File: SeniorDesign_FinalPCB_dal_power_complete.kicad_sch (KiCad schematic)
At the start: 75 parts, among them J1 5000, J10 5000, J2 5000, J3 5000, J4 5000, J5 5000, J6 5000, J7 5000, J8 5000, J9 5000, U1 Transducer, U10 Transducer, U11 Transducer, U12 Transducer, U13 Transducer, U14 Transducer, U15 Transducer, U16 Transducer, U17 Transducer, U18 Transducer, U19 Transducer, U2 Transducer, U20 Transducer, U21 Transducer, U22 Transducer, U23 Transducer, U24 Transducer, U25 Transducer, U26 Transducer, U27 Transducer, U28 Transducer, U29 Transducer, U3 Transducer, U30 Transducer, U31 Transducer, U32 Transducer, U33 Transducer, U34 Transducer, U35 Transducer, U36 Transducer, U37 Transducer, U38 Transducer, U39 Transducer, U4 Transducer, U40 Transducer, U41 Transducer, U42 Transducer, U43 Transducer, U44 Transducer, U45 Transducer, U46 Transducer, U47 Transducer, U48 Transducer, U49 Transducer, U5 Transducer, U50 Transducer, U51 Transducer, U52 Transducer, U53 Transducer, U54 Transducer, U55 Transducer, U56 Transducer, U57 Transducer, U58 Transducer, U59 Transducer, U6 Transducer, U60 Transducer, U61 Transducer, U62 Transducer, U63 Transducer, U64 Transducer, U65 CMOD_A7, U7 Transducer, U8 Transducer, U9 Transducer

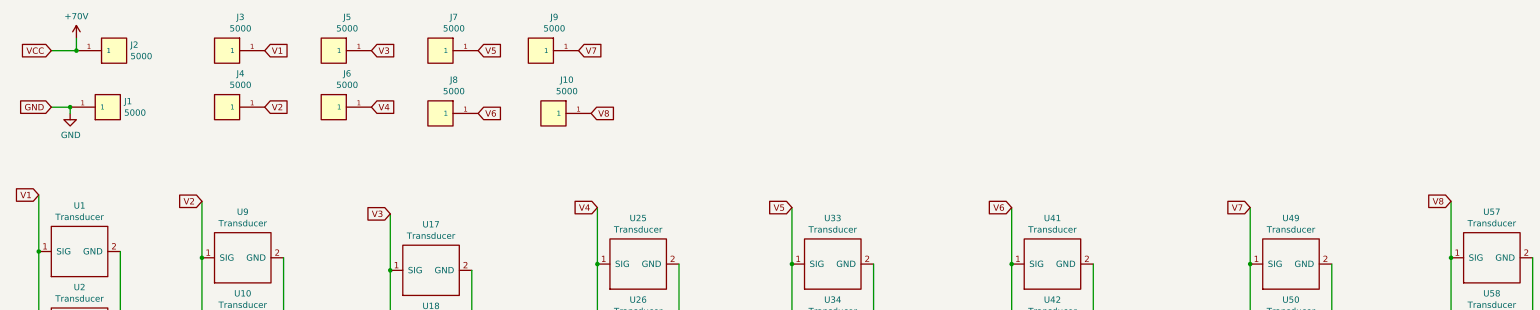
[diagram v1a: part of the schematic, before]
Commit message: Fixed transducer trace widths and via net names.
Also adds WELAC logo and silkscreen board name + contributors
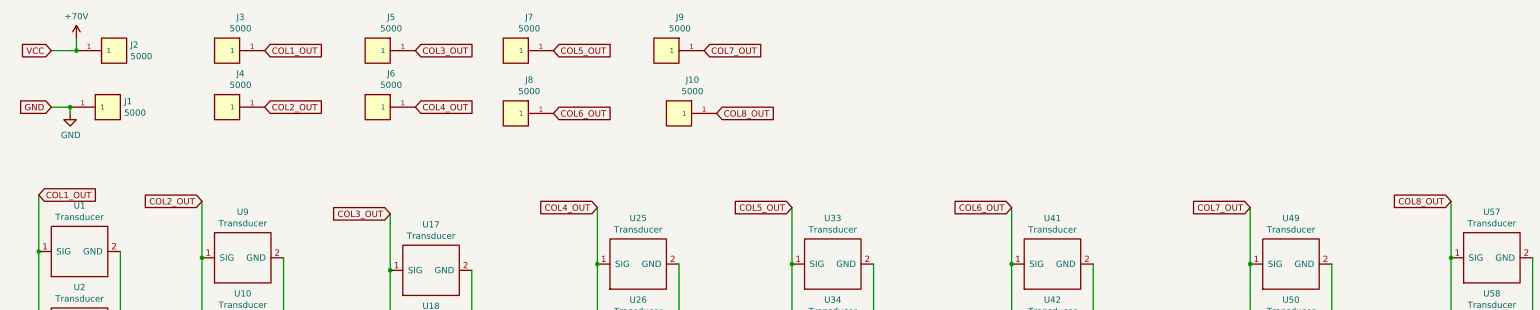
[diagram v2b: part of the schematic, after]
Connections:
- net V1 renamed COL1_OUT
- net V2 renamed COL2_OUT
- net V3 renamed COL3_OUT
- net V4 renamed COL4_OUT
- net V5 renamed COL5_OUT
- net V6 renamed COL6_OUT
- net V7 renamed COL7_OUT
- net V8 renamed COL8_OUT
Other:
- moved on the sheet: J10, J5, J6, J7, J8, J9

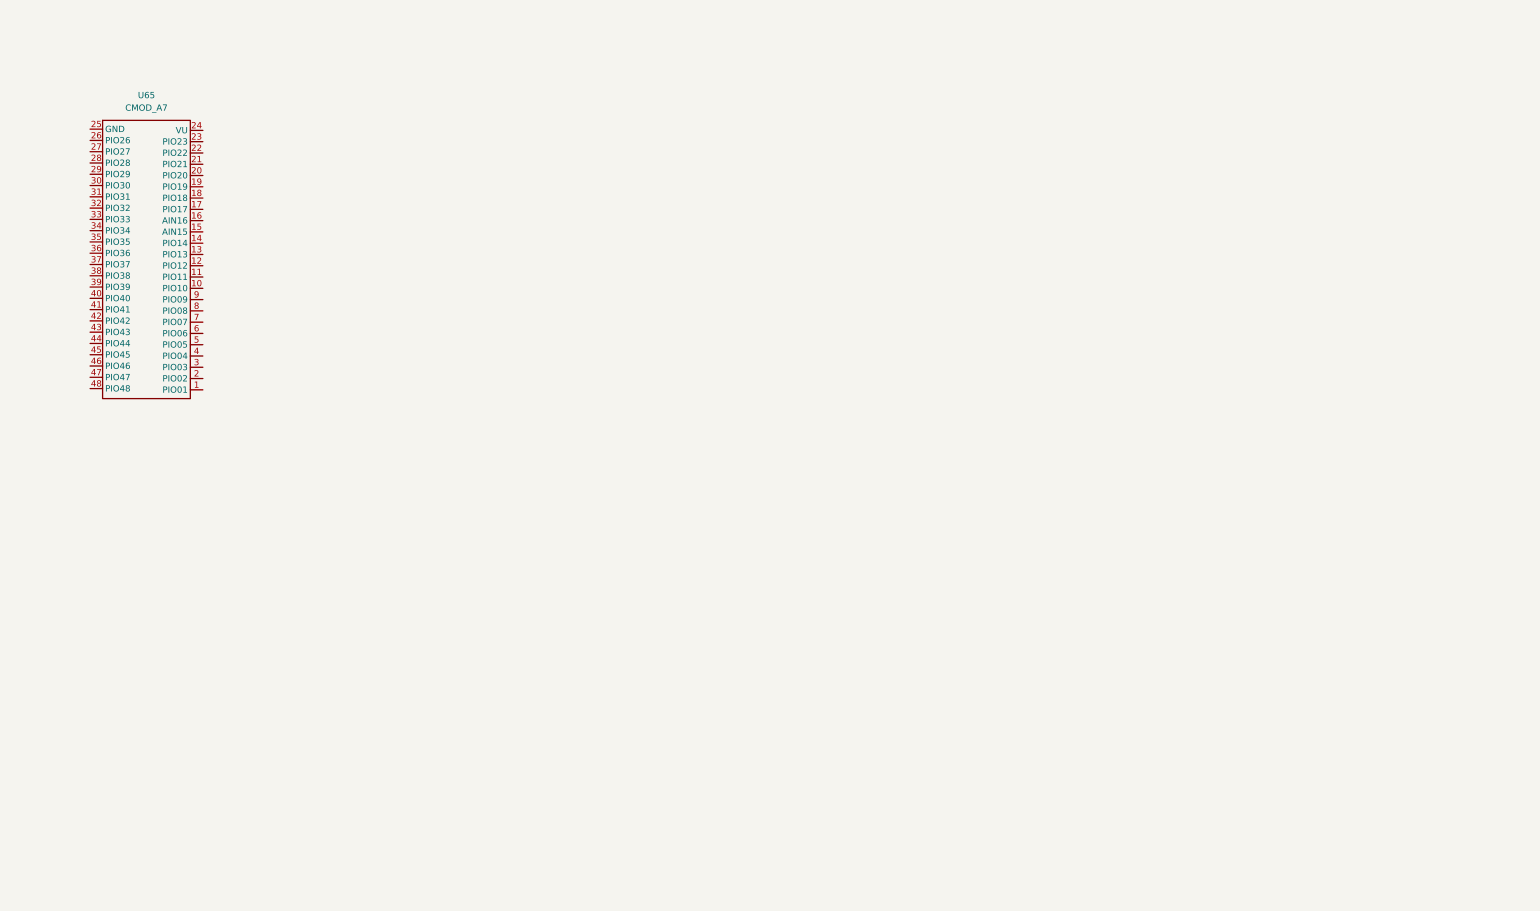
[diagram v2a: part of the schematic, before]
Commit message: all major components added, routing underway
added and fixed some component footprints. routed column signals and designed/layout of audio amplifier and power supply. NEED TO CHECK CAP VOLTAGES
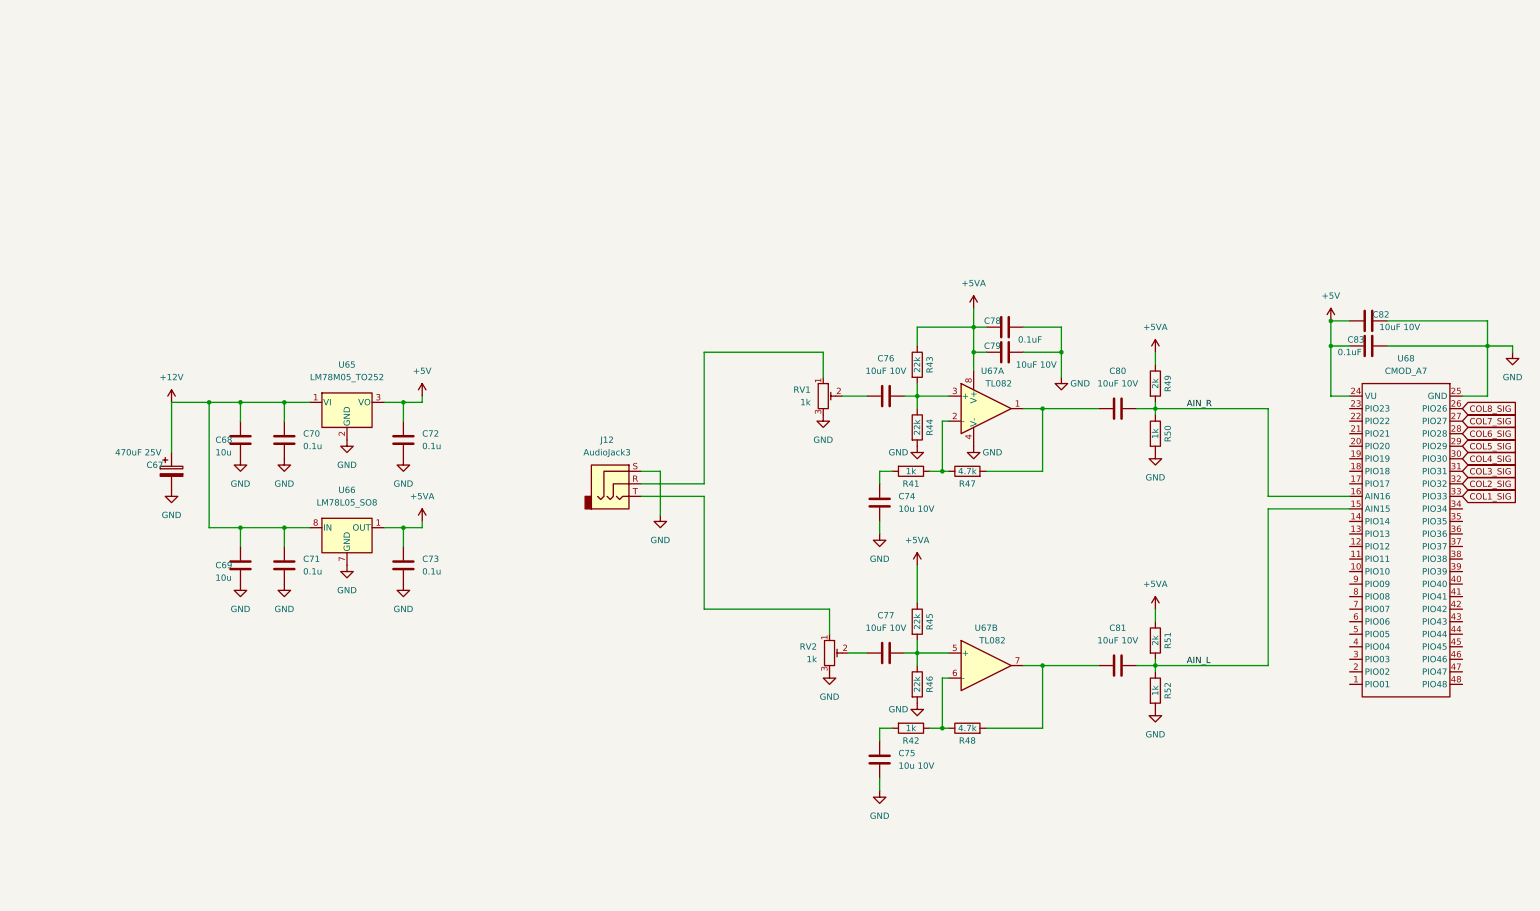
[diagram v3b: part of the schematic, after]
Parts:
- removed U65: CMOD_A7, SeniorDesign:CMOD A7, symbol SeniorDesign:CMOD_A7
- added C67: 470uF 25V, Capacitor_SMD:CP_Elec_10x10, symbol Device:C_Polarized
- added C68, C69: 10u, Capacitor_SMD:C_0603_1608Metric, symbol Device:C
- added C70, C71, C72, C73: 0.1u, Capacitor_SMD:C_0603_1608Metric, symbol Device:C
- added C74, C75: 10u 10V, Capacitor_SMD:C_0603_1608Metric, symbol Device:C
- added C76, C77, C79, C80, C81, C82: 10uF 10V, Capacitor_SMD:C_0603_1608Metric, symbol Device:C
- added C78, C83: 0.1uF, Capacitor_SMD:C_0603_1608Metric, symbol Device:C
- added J12: AudioJack3, Connector_Audio:Jack_3.5mm_CUI_SJ-3523-SMT_Horizontal, symbol Connector:AudioJack3
- added R41, R42, R50, R52: 1k, Resistor_SMD:R_0603_1608Metric, symbol Device:R
- added R43, R44, R45, R46: 22k, Resistor_SMD:R_0603_1608Metric, symbol Device:R
- added R47, R48: 4.7k, Resistor_SMD:R_0603_1608Metric, symbol Device:R
- added R49, R51: 2k, Resistor_SMD:R_0603_1608Metric, symbol Device:R
- added RV1, RV2: 1k, Potentiometer_SMD:Potentiometer_Bourns_3314J_Vertical, symbol Device:R_Potentiometer_Trim
- added U65: LM78M05_TO252, Package_TO_SOT_SMD:TO-252-2, symbol Regulator_Linear:LM78M05_TO252
- added U66: LM78L05_SO8, Package_SO:SOIC-8_3.9x4.9mm_P1.27mm, symbol Regulator_Linear:LM78L05_SO8
- added U67: TL082, Package_DIP:DIP-8_W7.62mm_LongPads, symbol Amplifier_Operational:TL082
- added U68: CMOD_A7, Senior:CMOD A7, symbol SeniorDesign:CMOD_A7
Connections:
- net GND: now also C67.2, C68.2, C69.2, C70.2, C71.2, C72.2, C73.2, C74.1, C75.1, C78.2, C79.2, C82.2, C83.2, J12.S, R44.2, R46.2, R50.2, R52.2, RV1.3, RV2.3, U65.2 (GND), U66.2 (GND), U66.3 (GND), U66.6 (GND), U66.7 (GND), U67.4 (V-), U68.25 (GND)
- new net: C81.1, R48.2, U67.7
- new net: R42.1, R48.1, U67.6 (-)
- new net: C77.2, R45.2, R46.1, U67.5 (+)
- new net: C76.2, R43.2, R44.1, U67.3 (+)
- new net: C80.1, R47.2, U67.1
- new net: R41.1, R47.1, U67.2 (-)
- new net: C77.1, RV2.2
- new net: J12.R, RV1.1
- new net: C76.1, RV1.2
- new net: C74.2, R41.2
- new net: C75.2, R42.2
- new net: J12.T, RV2.1
- new net +12V: C67.1, C68.1, C69.1, C70.1, C71.1, U65.1 (VI), U66.8 (IN)
- new net +5V: C72.1, C82.1, C83.1, U65.3 (VO), U68.24 (VU)
- new net +5VA: C73.1, C78.1, C79.1, R43.1, R45.1, R49.1, R51.1, U66.1 (OUT), U67.8 (V+)
- new net AIN_L: C81.2, R51.2, R52.1, U68.15 (AIN15)
- new net AIN_R: C80.2, R49.2, R50.1, U68.16 (AIN16)
- new net COL1_SIG: U68.33 (PIO33)
- new net COL2_SIG: U68.32 (PIO32)
- new net COL3_SIG: U68.31 (PIO31)
- new net COL4_SIG: U68.30 (PIO30)
- new net COL5_SIG: U68.29 (PIO29)
- new net COL6_SIG: U68.28 (PIO28)
- new net COL7_SIG: U68.27 (PIO27)
- new net COL8_SIG: U68.26 (PIO26)

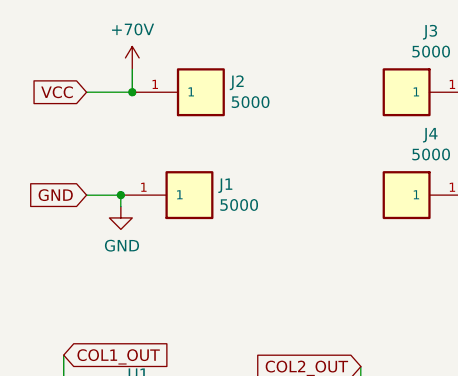
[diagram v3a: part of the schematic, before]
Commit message: Add 3D Models, Adjust components, Minor changes
- Footprint for 1206 Capacitors is in the footprints folder
- Added a mostly correct size transducer 3D model
- Added the 3D model for the screw terminal
- The above models are in a new folder called SeniorDesign_3DModels
- Fixed some component placements and silkscreens that overlapped
- Added 3D models for all resistors and capacitors of the power circuits
- Fixed the VCC testpoint to be VPP
- Adjusted the Transducer footprint to be 16.3mm in diameter in the event it is deemed necessary to change the spacing of the transducers to make sure they dont interfere with each other
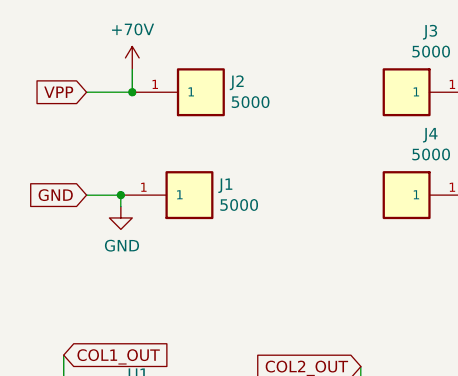
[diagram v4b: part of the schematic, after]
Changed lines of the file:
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@@
     )
   )
-  (global_label "VCC" (shape input) (at 21.59 22.86 180) (fields_autoplaced)
+  (global_label "VPP" (shape input) (at 21.59 22.86 180) (fields_autoplaced)
     (effects (font (size 1.27 1.27)) (justify right))
-    (property "Intersheet References" "${INTERSHEET_REFS}" (id 0) (at 0 0 0)
-      (effects (font (size 1.27 1.27)) hide)
+    (property "Intersheet References" "${INTERSHEET_REFS}" (id 0) (at 15.6372 22.7806 0)
+      (effects (font (size 1.27 1.27)) (justify right) hide)
     )
   )

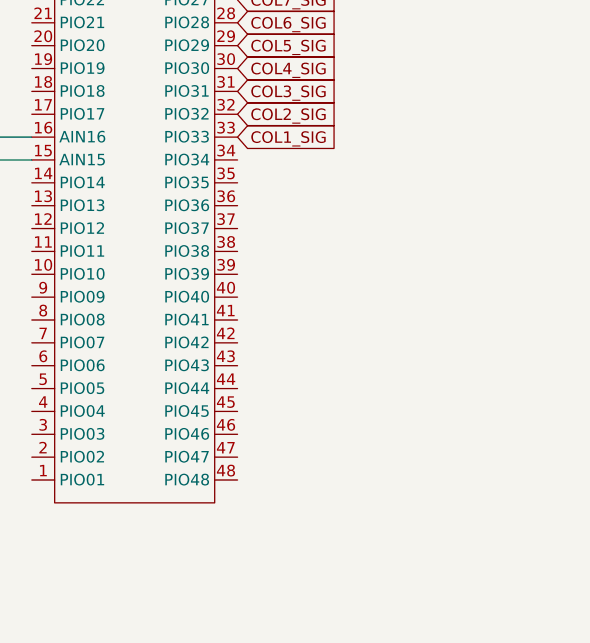
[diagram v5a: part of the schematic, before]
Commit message: final pre-design review push
Fixed some routing problems. Changed capacitor sizes for large bypass voltages. array modeled
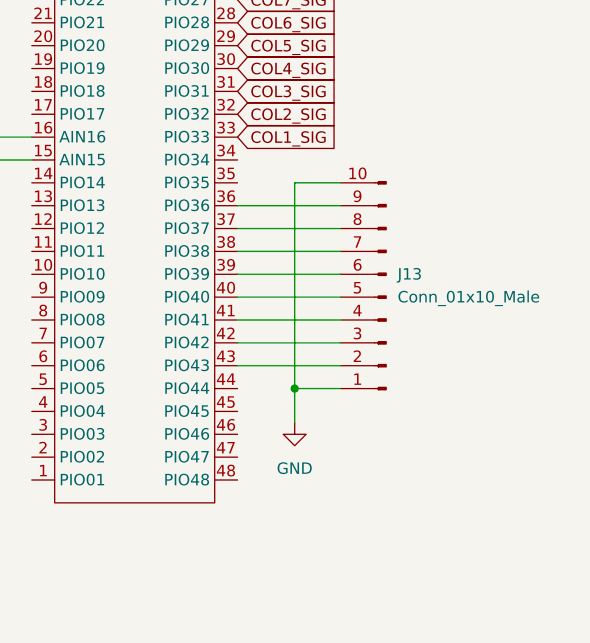
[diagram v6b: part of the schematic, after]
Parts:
- added J13: Conn_01x10_Male, Connector_PinHeader_2.54mm:PinHeader_1x10_P2.54mm_Vertical, symbol Connector:Conn_01x10_Male
- U1, U10, U11, U12, U13, U14, U15, U16, U17, U18, U19, U2, U20, U21, U22, U23, U24, U25, U26, U27, U28, U29, U3, U30, U31, U32, U33, U34, U35, U36, U37, U38, U39, U4, U40, U41, U42, U43, U44, U45, U46, U47, U48, U49, U5, U50, U51, U52, U53, U54, U55, U56, U57, U58, U59, U6, U60, U61, U62, U63, U64, U7, U8, U9: footprint SeniorDesign:Transducer -> Senior:Transducer
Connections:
- net GND: now also J13.1 (Pin_1), J13.10 (Pin_10)
- net at U68.36 (PIO36): now also J13.9 (Pin_9)
- net at U68.37 (PIO37): now also J13.8 (Pin_8)
- net at U68.38 (PIO38): now also J13.7 (Pin_7)
- net at U68.39 (PIO39): now also J13.6 (Pin_6)
- net at U68.40 (PIO40): now also J13.5 (Pin_5)
- net at U68.41 (PIO41): now also J13.4 (Pin_4)
- net at U68.42 (PIO42): now also J13.3 (Pin_3)
- net at U68.43 (PIO43): now also J13.2 (Pin_2)

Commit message: final send out
sent out week of 2/28
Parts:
- removed J1, J2: 5000, SeniorDesign:KEYSTONE_5000_TestPoint, symbol SeniorDesign:5000
- R49, R51: value 2k -> 1.5k
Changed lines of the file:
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@@
   (junction (at 321.31 167.64) (diameter 0) (color 0 0 0 0)
   )
-  (junction (at 25.4 34.29) (diameter 0) (color 0 0 0 0)
-  )
   (junction (at 321.31 115.57) (diameter 0) (color 0 0 0 0)
   )
@@
   (junction (at 132.08 82.55) (diameter 0) (color 0 0 0 0)
   )
-  (junction (at 26.67 22.86) (diameter 0) (color 0 0 0 0)
-  )
   (junction (at 591.82 125.73) (diameter 0) (color 0 0 0 0)
   )
@@
     (pin "~")
   )
-  (symbol (lib_id "SeniorDesign:5000") (at 34.29 22.86 0) (unit 1)
-    (in_bom yes) (on_board yes)
-    (property "Reference" "J2" (id 0) (at 37.592 21.6916 0)
-      (effects (font (size 1.27 1.27)) (justify left))
-    )
-    (property "Value" "5000" (id 1) (at 37.592 24.003 0)
-      (effects (font (size 1.27 1.27)) (justify left))
-    )
-    (property "Footprint" "SeniorDesign:KEYSTONE_5000_TestPoint" (id 2) (at 30.48 29.21 0)
-      (effects (font (size 1.27 1.27)) (justify left bottom) hide)
-    )
-    (property "Datasheet" "" (id 3) (at 34.29 22.86 0)
-      (effects (font (size 1.27 1.27)) (justify left bottom) hide)
-    )
-    (property "MANUFACTURER" "KEYSTONE" (id 4) (at 30.48 29.21 0)
-      (effects (font (size 1.27 1.27)) (justify left bottom) hide)
-    )
-    (property "MAXIMUM_PACKAGE_HEIGHT" "4.57mm" (id 5) (at 22.86 29.21 0)
-      (effects (font (size 1.27 1.27)) (justify left bottom) hide)
-    )
-    (pin "1")
-  )
-  (symbol (lib_id "SeniorDesign:5000") (at 33.02 34.29 0) (unit 1)
-    (in_bom yes) (on_board yes)
-    (property "Reference" "J1" (id 0) (at 36.322 33.1216 0)
-      (effects (font (size 1.27 1.27)) (justify left))
-    )
-    (property "Value" "5000" (id 1) (at 36.322 35.433 0)
-      (effects (font (size 1.27 1.27)) (justify left))
-    )
-    (property "Footprint" "SeniorDesign:KEYSTONE_5000_TestPoint" (id 2) (at 29.21 40.64 0)
-      (effects (font (size 1.27 1.27)) (justify left bottom) hide)
-    )
-    (property "Datasheet" "" (id 3) (at 33.02 34.29 0)
-      (effects (font (size 1.27 1.27)) (justify left bottom) hide)
-    )
-    (property "MANUFACTURER" "KEYSTONE" (id 4) (at 29.21 40.64 0)
-      (effects (font (size 1.27 1.27)) (justify left bottom) hide)
-    )
-    (property "MAXIMUM_PACKAGE_HEIGHT" "4.57mm" (id 5) (at 21.59 40.64 0)
-      (effects (font (size 1.27 1.27)) (justify left bottom) hide)
-    )
-    (pin "1")
-  )
   (symbol (lib_id "SeniorDesign:Transducer") (at 21.59 68.58 0) (unit 1)
     (in_bom yes) (on_board yes)
@@
     (in_bom yes) (on_board yes)
     (property "Reference" "R49" (id 0) (at 637.54 107.95 90))
-    (property "Value" "2k" (id 1) (at 635 107.95 90))
+    (property "Value" "1.5k" (id 1) (at 635 107.95 90))
     (property "Footprint" "Resistor_SMD:R_0603_1608Metric" (id 2) (at 633.222 107.95 90)
       (effects (font (size 1.27 1.27)) hide)
@@
     (in_bom yes) (on_board yes)
     (property "Reference" "R51" (id 0) (at 637.54 160.02 90))
-    (property "Value" "2k" (id 1) (at 635 160.02 90))
+    (property "Value" "1.5k" (id 1) (at 635 160.02 90))
     (property "Footprint" "Resistor_SMD:R_0603_1608Metric" (id 2) (at 633.222 160.02 90)
       (effects (font (size 1.27 1.27)) hide)
@@
       (reference "D16") (unit 1) (value "ER3GTR") (footprint "Diode_SMD:D_SMC")
     )
-    (path "/00000000-0000-0000-0000-0000618cbefd"
-      (reference "J1") (unit 1) (value "5000") (footprint "SeniorDesign:KEYSTONE_5000_TestPoint")
-    )
-    (path "/00000000-0000-0000-0000-0000618cae06"
-      (reference "J2") (unit 1) (value "5000") (footprint "SeniorDesign:KEYSTONE_5000_TestPoint")
-    )
     (path "/00000000-0000-0000-0000-0000619831bd"
       (reference "J3") (unit 1) (value "5000") (footprint "SeniorDesign:KEYSTONE_5000_TestPoint")
@@
     )
     (path "/0140c5fc-fa22-4dcb-bd3a-e8db2d9ce361"
-      (reference "R49") (unit 1) (value "2k") (footprint "Resistor_SMD:R_0603_1608Metric")
+      (reference "R49") (unit 1) (value "1.5k") (footprint "Resistor_SMD:R_0603_1608Metric")
     )
     (path "/425a0030-d494-4c3f-bff3-b628e2d2d578"
@@
     )
     (path "/ff3c7bc6-8e2c-4e57-994a-48bad797161a"
-      (reference "R51") (unit 1) (value "2k") (footprint "Resistor_SMD:R_0603_1608Metric")
+      (reference "R51") (unit 1) (value "1.5k") (footprint "Resistor_SMD:R_0603_1608Metric")
     )
     (path "/1e5b3e84-3623-4283-8e60-30db8251c3c8"
